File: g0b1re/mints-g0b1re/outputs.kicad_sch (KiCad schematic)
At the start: 50 parts, among them Q1 SQM120P06-07L_GE3, Q2 SQM120P06-07L_GE3, Q3 SQM120P06-07L_GE3, Q4 SQM120P06-07L_GE3, Q5 SQM120P06-07L_GE3, Q6 SQM120P06-07L_GE3, Q7 SQM120P06-07L_GE3, Q8 SQM120P06-07L_GE3, U201 140357145200, U202 140357145200, U203 140357145200, U204 140357145200, U205 140357145200, U206 140357145200, U207 140357145200, U208 140357145200

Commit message: polishing schematic, add variants, fix some small issues
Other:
- note added: "Output Current Limit Each: Max 2.8A continous @ 15C board above ambient Max 6A peak inrush Combined Max 13A continous @ 15C board above ambient"
- note added: "Outputs are electrically isolated"
- note added: "Would be nice to use KiCad MOSFET Symbol BE CAREFUL OF GDS CONNECTIONS"
- note removed: "pick better fet P channel MOSFET 60v 15A lowest on resistance you can"
- company: (none) -> Portland State Aerospace Society
- title: (none) -> minTS SCADA Board

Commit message: board updates 9/2/26
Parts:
- added RN205, RN206: 5k1, Resistor_SMD:R_Array_Convex_4x0603, symbol Device:R_Pack04_Split
- Q1, Q2, Q3, Q4, Q5, Q6, Q7, Q8: footprint SQM120P06-07L_GE3:TO-263_SQM120P06-07L_GE3_VIS -> LIB_DMP6023LFGQ-7:DMTH8008LFGQ7
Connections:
- net GNDP: now also U203.4, RN205.7 (R2.2)
- net ~{ISO_OUT_0}: now also RN205.5 (R4.2); no longer Q1.1 (G), RN203.5 (R4.2)
- net ~{ISO_OUT_1}: now also RN205.6 (R3.2); no longer Q2.1 (G), RN203.6 (R3.2)
- net ~{ISO_OUT_3}: now also RN205.8 (R1.2); no longer Q8.1 (G), RN203.8 (R1.2)
- net ~{ISO_OUT_4}: now also RN206.5 (R4.2); no longer Q4.1 (G), RN204.5 (R4.2)
- net ~{ISO_OUT_5}: now also RN206.6 (R3.2); no longer Q5.1 (G), RN204.6 (R3.2)
- net ~{ISO_OUT_6}: now also RN206.7 (R2.2); no longer Q6.1 (G), RN204.7 (R2.2)
- net ~{ISO_OUT_7}: now also RN206.8 (R1.2); no longer Q7.1 (G), RN204.8 (R1.2)
- removed net ~{ISO_OUT_2}: Q3.1 (G), RN203.7 (R2.2), U203.4
- new net: Q8.1 (G), RN203.8 (R1.2), RN205.1 (R1.1)
- new net: Q5.1 (G), RN204.6 (R3.2), RN206.3 (R3.1)
- new net: Q1.1 (G), RN203.5 (R4.2), RN205.4 (R4.1)
- new net: RN203.7 (R2.2), RN205.2 (R2.1)
- new net: Q2.1 (G), RN203.6 (R3.2), RN205.3 (R3.1)
- new net: Q7.1 (G), RN204.8 (R1.2), RN206.1 (R1.1)
- new net: Q4.1 (G), RN204.5 (R4.2), RN206.4 (R4.1)
- new net: Q6.1 (G), RN204.7 (R2.2), RN206.2 (R2.1)
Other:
- moved on the sheet: RN203B, RN203D, RN204B, RN204D

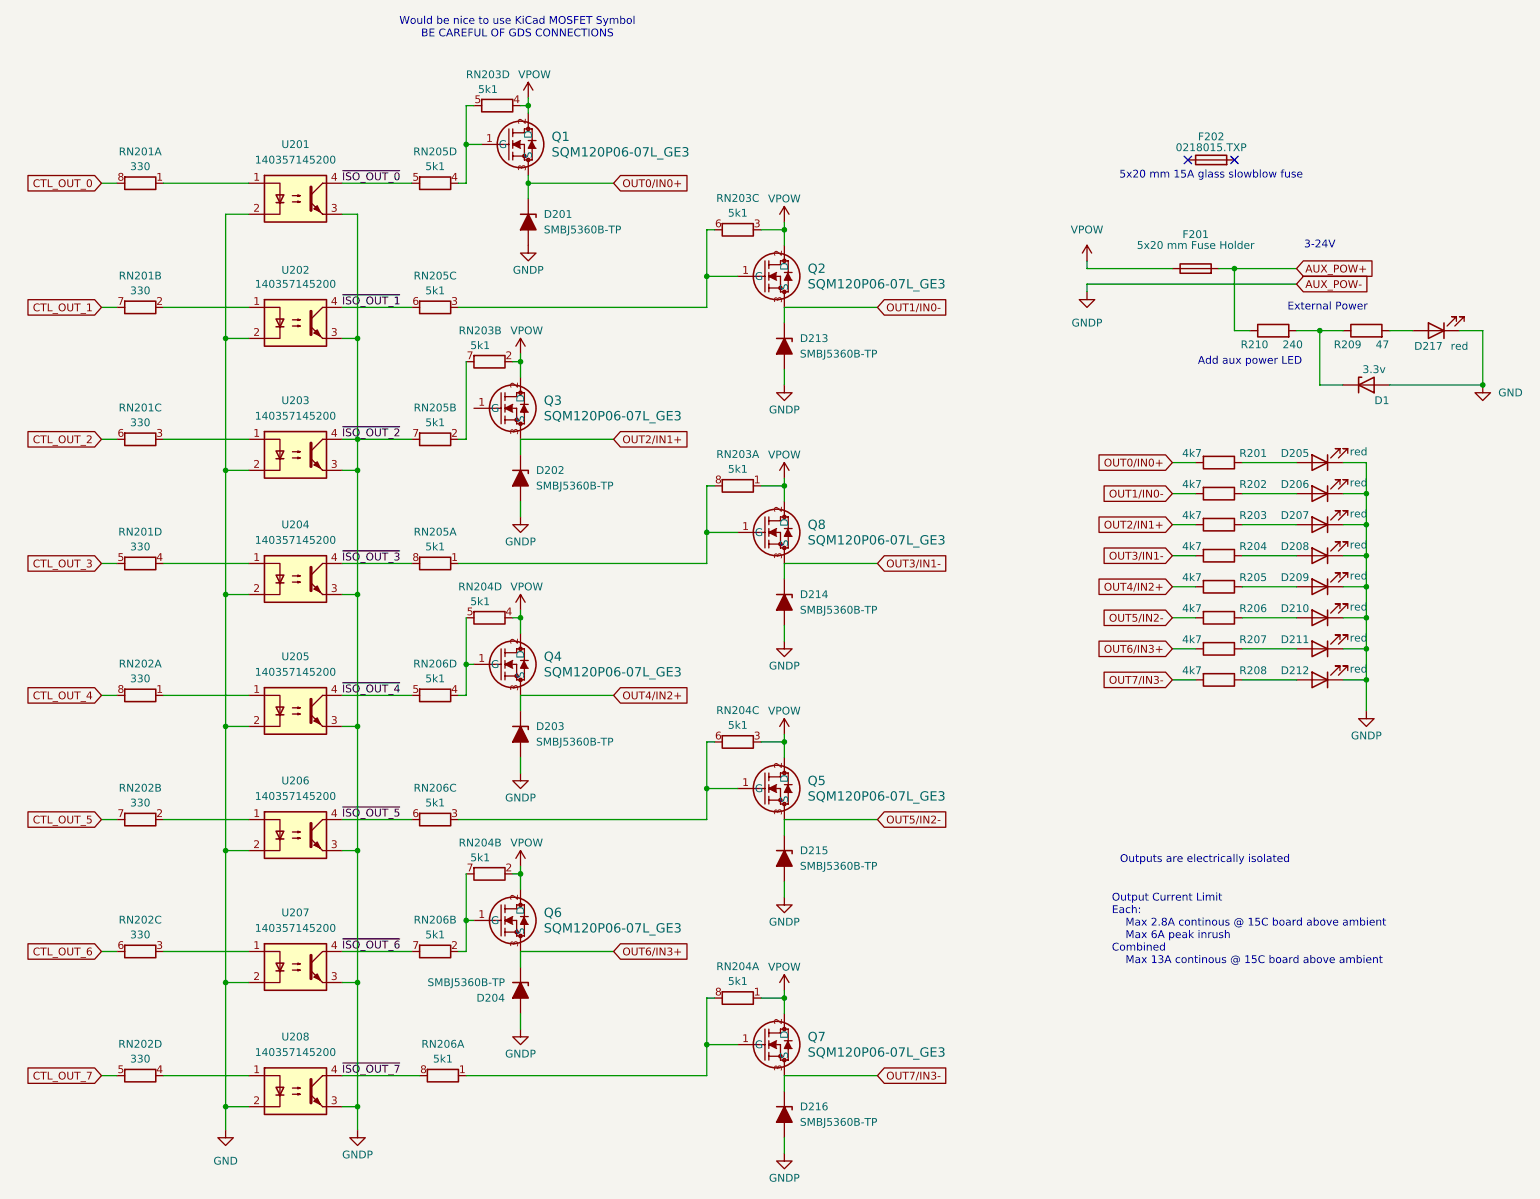
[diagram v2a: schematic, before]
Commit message: finneshed trace routing; fixed DRC errors
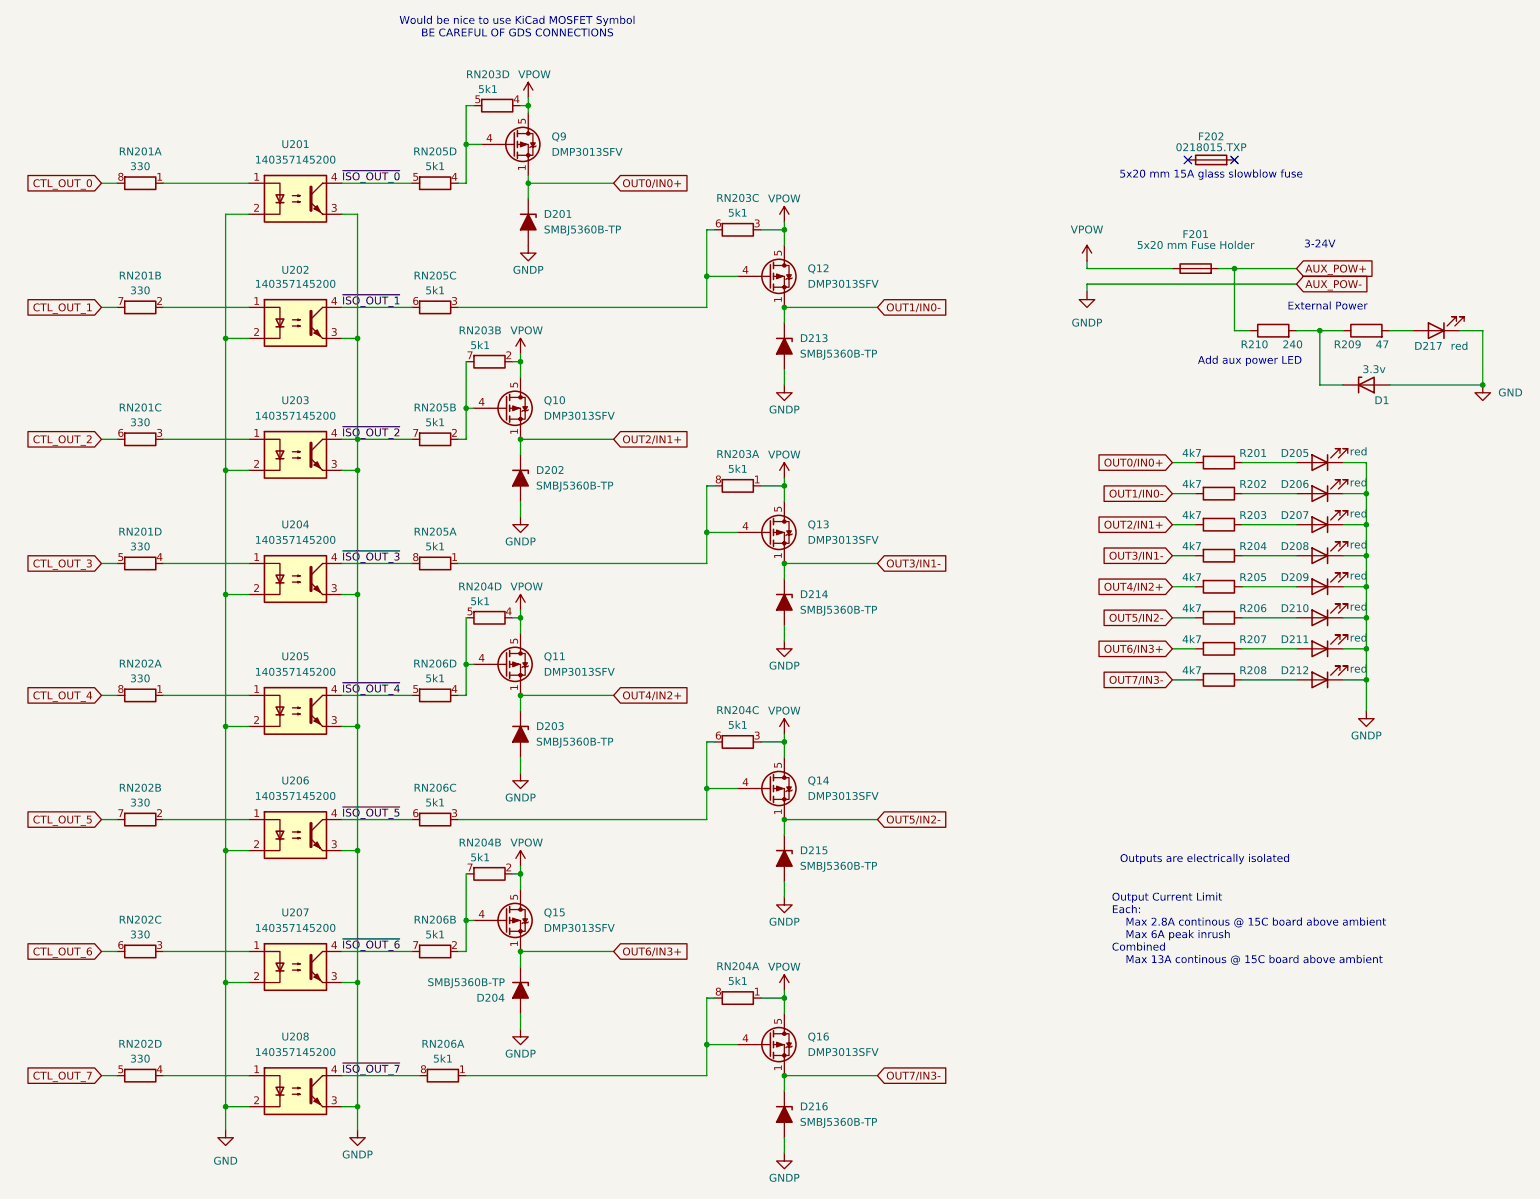
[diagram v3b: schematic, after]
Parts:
- removed Q1, Q2, Q3, Q4, Q5, Q6, Q7, Q8: SQM120P06-07L_GE3, LIB_DMP6023LFGQ-7:DMTH8008LFGQ7, symbol 2026-07-27_21-07-26:SQM120P06-07L_GE3
- added Q10, Q11, Q12, Q13, Q14, Q15, Q16, Q9: DMP3013SFV, Package_SON:Diodes_PowerDI3333-8, symbol Transistor_FET:DMP3013SFV
- D201, D202, D203, D204, D213, D214, D215, D216: footprint Diode_SMD:D_SMB -> SZMMSZ5258BT3G:SOD-123_ONS
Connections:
- net OUT0/IN0+: now also Q9.1 (S), Q9.2 (S), Q9.3 (S)
- net OUT1/IN0-: now also Q12.1 (S), Q12.2 (S), Q12.3 (S)
- net OUT2/IN1+: now also Q10.1 (S), Q10.2 (S), Q10.3 (S)
- net OUT3/IN1-: now also Q13.1 (S), Q13.2 (S), Q13.3 (S)
- net OUT4/IN2+: now also Q11.1 (S), Q11.2 (S), Q11.3 (S)
- net OUT5/IN2-: now also Q14.1 (S), Q14.2 (S), Q14.3 (S)
- net OUT6/IN3+: now also Q15.1 (S), Q15.2 (S), Q15.3 (S)
- net OUT7/IN3-: now also Q16.1 (S), Q16.2 (S), Q16.3 (S)
- net VPOW: now also Q10.5 (D), Q11.5 (D), Q12.5 (D), Q13.5 (D), Q14.5 (D), Q15.5 (D), Q16.5 (D), Q9.5 (D)
- net at RN203.8 (R1.2), RN205.1 (R1.1): now also Q13.4 (G)
- net at RN204.6 (R3.2), RN206.3 (R3.1): now also Q14.4 (G)
- net at RN203.5 (R4.2), RN205.4 (R4.1): now also Q9.4 (G)
- net at RN203.7 (R2.2), RN205.2 (R2.1): now also Q10.4 (G)
- net at RN203.6 (R3.2), RN205.3 (R3.1): now also Q12.4 (G)
- net at RN204.8 (R1.2), RN206.1 (R1.1): now also Q16.4 (G)
- net at RN204.5 (R4.2), RN206.4 (R4.1): now also Q11.4 (G)
- net at RN204.7 (R2.2), RN206.2 (R2.1): now also Q15.4 (G)
